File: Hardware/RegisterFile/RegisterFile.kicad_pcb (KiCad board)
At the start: 4 copper layers, 94 x 66 mm, 39 parts, among them J1 Conn_02x08_Odd_Even, J2 Conn_02x08_Odd_Even, J3 Conn_02x08_Odd_Even, J4 Conn_02x08_Odd_Even, U1 74LS138

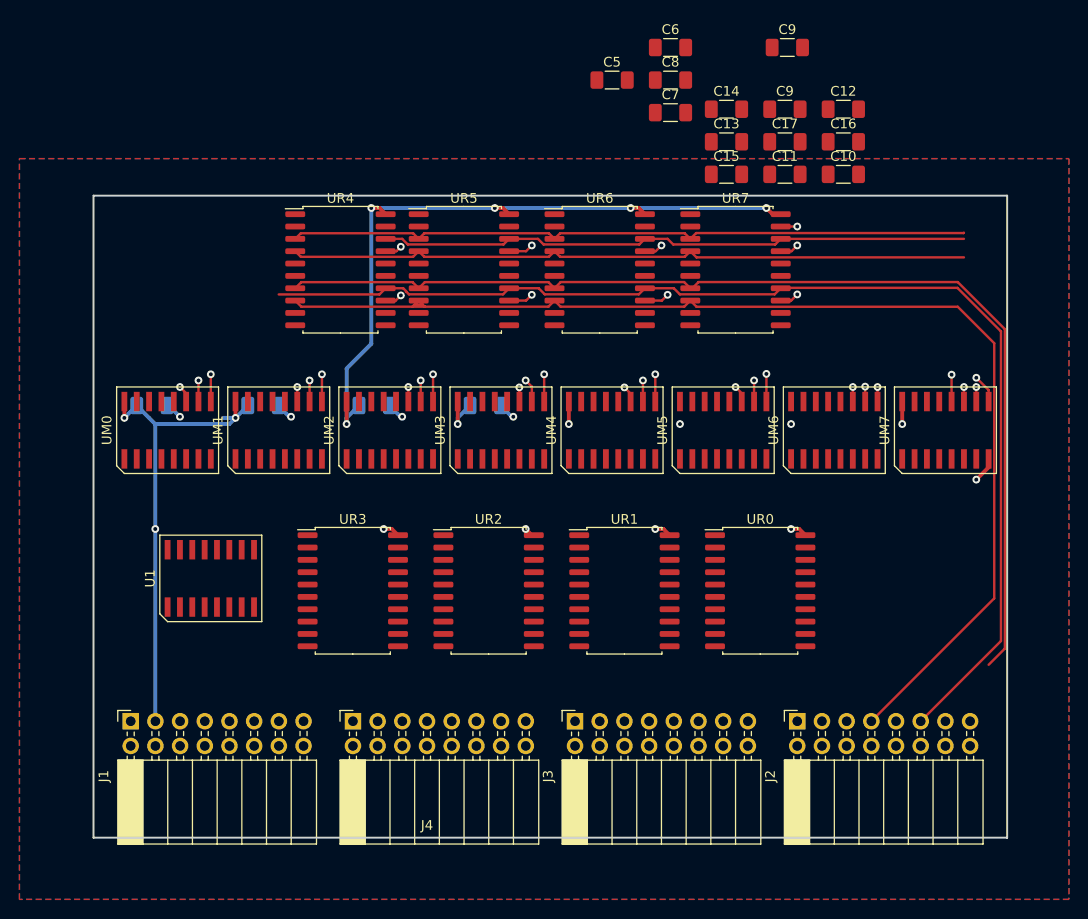
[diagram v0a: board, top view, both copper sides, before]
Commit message: RegisterFile Layout: Everything except the "spider" (routing the all 8 muxes each to all 8 registers might be non-trivial)
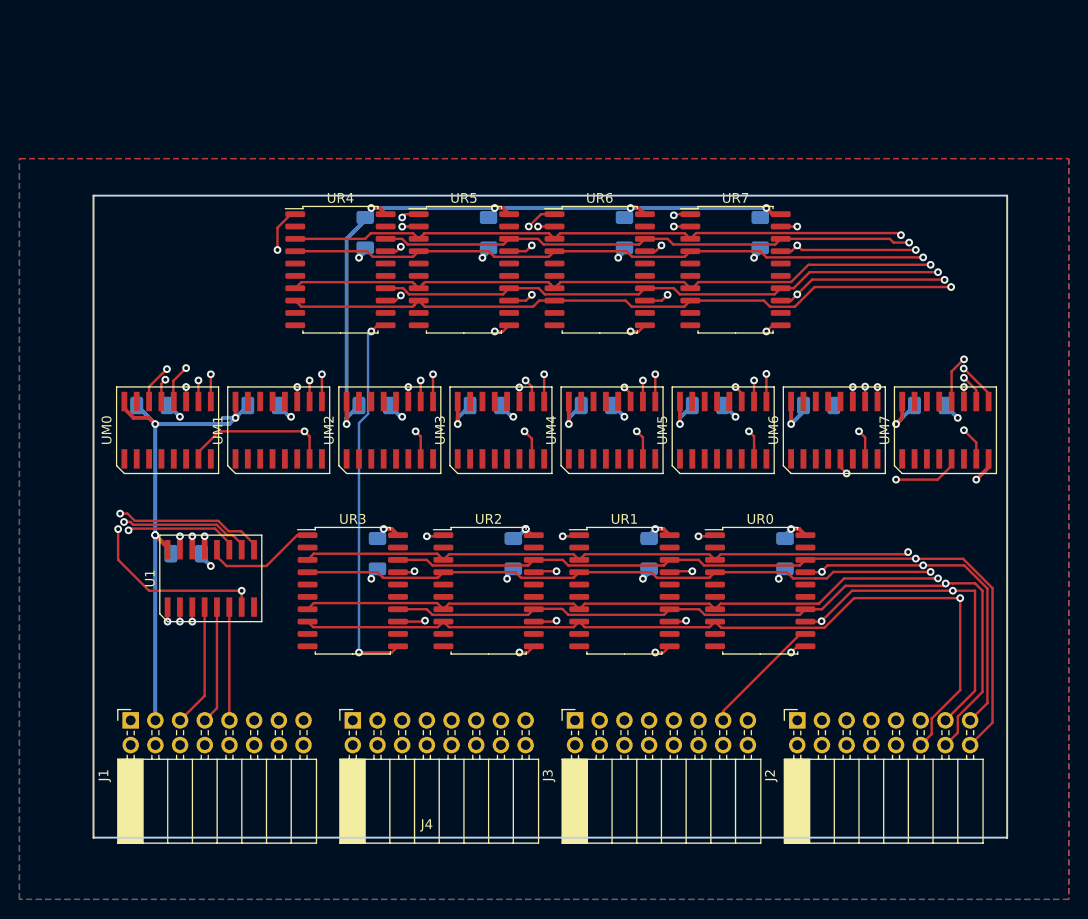
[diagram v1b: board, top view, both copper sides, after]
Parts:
- removed the C9 at (167.9, 52.1)
- removed the C9 at (167.6, 58.4)
- added C9: .1uF, Capacitor_SMD:C_1206_3216Metric_Pad1.33x1.80mm_HandSolder, B.Cu at (125.7, 104.1)
- C10, C11, C12, C13, C14, C15, C16, C17, C5, C6, C7, C8: moved to B.Cu
- moved C17 74.8 mm to (106.0, 104.1)
- moved C10 51.7 mm to (139.7, 104.1), turned to -90 degrees
- moved C12 46.1 mm to (167.6, 104.1), turned to -90 degrees
- moved C8 42.8 mm to (182.5, 88.9)
- moved C11 41.4 mm to (153.7, 104.1), turned to -90 degrees
- moved C13 38.3 mm to (124.5, 71.1), turned to -90 degrees
- moved C6 37.0 mm to (159.7, 88.9)
- moved C7 33.8 mm to (171.1, 88.9)
- moved C5 33.5 mm to (148.2, 88.9)
- moved C14 27.6 mm to (137.2, 71.1), turned to -90 degrees
- moved C16 12.7 mm to (165.1, 71.1), turned to -90 degrees
- moved C15 12.1 mm to (151.1, 71.1), turned to -90 degrees
- moved J4 0.09 mm to (123.2, 121.3)
- moved J1 0.09 mm to (100.3, 121.3)
- moved J2 0.09 mm to (168.9, 121.3)
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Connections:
- J2 pad 1: /DATAIN0 -> /DATAOUT0
- J2 pad 10: /DATAOUT4 -> /DATAIN1
- J2 pad 11: /DATAIN5 -> /DATAIN2
- J2 pad 12: /DATAOUT5 -> /DATAIN3
- J2 pad 13: /DATAIN6 -> /DATAIN4
- J2 pad 14: /DATAOUT6 -> /DATAIN5
- J2 pad 15: /DATAIN7 -> /DATAIN6
- J2 pad 16: /DATAOUT7 -> /DATAIN7
- J2 pad 2: /DATAOUT0 -> /DATAOUT1
- J2 pad 3: /DATAIN1 -> /DATAOUT2
- J2 pad 4: /DATAOUT1 -> /DATAOUT3
- J2 pad 5: /DATAIN2 -> /DATAOUT4
- J2 pad 6: /DATAOUT2 -> /DATAOUT5
- J2 pad 7: /DATAIN3 -> /DATAOUT6
- J2 pad 8: /DATAOUT3 -> /DATAOUT7
- J2 pad 9: /DATAIN4 -> /DATAIN0
- J3 pad 1: /REG0_0 -> /REG1_0
- J3 pad 10: /REG1_4 -> /REG0_1
- J3 pad 11: /REG0_5 -> /REG0_2
- J3 pad 12: /REG1_5 -> /REG0_3
- J3 pad 13: /REG0_6 -> /REG0_4
- J3 pad 14: /REG1_6 -> /REG0_5
- J3 pad 15: /REG0_7 -> /REG0_6
- J3 pad 16: /REG1_7 -> /REG0_7
- J3 pad 2: /REG1_0 -> /REG1_1
- J3 pad 3: /REG0_1 -> /REG1_2
- J3 pad 4: /REG1_1 -> /REG1_3
- J3 pad 5: /REG0_2 -> /REG1_4
- J3 pad 6: /REG1_2 -> /REG1_5
- J3 pad 7: /REG0_3 -> /REG1_6
- J3 pad 8: /REG1_3 -> /REG1_7
- J3 pad 9: /REG0_4 -> /REG0_0
- J4 pad 1: /REG2_0 -> /REG3_0
- J4 pad 10: /REG3_4 -> /REG2_1
- J4 pad 11: /REG2_5 -> /REG2_2
- J4 pad 12: /REG3_5 -> /REG2_3
- J4 pad 13: /REG2_6 -> /REG2_4
- J4 pad 14: /REG3_6 -> /REG2_5
- J4 pad 15: /REG2_7 -> /REG2_6
- J4 pad 16: /REG3_7 -> /REG2_7
- J4 pad 2: /REG3_0 -> /REG3_1
- J4 pad 3: /REG2_1 -> /REG3_2
- J4 pad 4: /REG3_1 -> /REG3_3
- J4 pad 5: /REG2_2 -> /REG3_4
- J4 pad 6: /REG3_2 -> /REG3_5
- J4 pad 7: /REG2_3 -> /REG3_6
- J4 pad 8: /REG3_3 -> /REG3_7
- J4 pad 9: /REG2_4 -> /REG2_0
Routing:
- net /CLK: track 0.00 -> 148.8 mm, vias 0 -> 8
- net /DATAIN1: track 70.5 -> 184.3 mm, vias 0 -> 2
- net /DATAIN6: track 66.2 -> 177.4 mm, vias 4 -> 10
- net /Regs/~{WRITESEL7}: track 0.00 -> 110.3 mm, vias 0 -> 3
- net /DATAIN7: track 60.9 -> 169.3 mm, vias 0 -> 2
- net /DATAIN0: track 70.5 -> 178.5 mm, vias 0 -> 2
- net /~{REN}: track 0.00 -> 102.3 mm, vias 0 -> 7
- net /Regs/~{WRITESEL6}: track 0.00 -> 81.8 mm, vias 0 -> 2
- net /DATAIN2: track 112.0 -> 183.6 mm, vias 0 -> 2
- net /DATAIN3: track 121.6 -> 189.6 mm, vias 0 -> 2
- net /Regs/~{WRITESEL5}: track 0.00 -> 64.8 mm, vias 0 -> 2
- net /DATAIN4: track 114.9 -> 179.2 mm, vias 4 -> 10
- net /REG7_0: track 0.00 -> 62.2 mm, vias 0 -> 2
- net /Regs/~{WRITESEL0}: track 0.00 -> 57.5 mm, vias 0 -> 2
- net /Regs/~{WRITESEL4}: track 0.00 -> 51.8 mm, vias 0 -> 2
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
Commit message: RegisterFile: The layout's all done!
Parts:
- added C18: .1uF, Capacitor_SMD:C_1206_3216Metric_Pad1.33x1.80mm_HandSolder, B.Cu at (101.6, 118.7)
- added C19: .1uF, Capacitor_SMD:C_1206_3216Metric_Pad1.33x1.80mm_HandSolder, B.Cu at (116.5, 118.7)
- J1, J2, J3, J4: footprint Connector_PinSocket_2.54mm:PinSocket_2x08_P2.54mm_Horizontal -> Connector_PinHeader_2.54mm:PinHeader_2x08_P2.54mm_Horizontal
- moved J2 17.8 mm to (186.7, 121.3), turned to -90 degrees
- moved J3 17.8 mm to (163.8, 121.3), turned to -90 degrees
- moved J4 17.8 mm to (141.0, 121.3), turned to -90 degrees
- moved J1 17.8 mm to (118.1, 121.3), turned to -90 degrees
- moved C12 6.35 mm to (174.0, 104.1)
- moved UR0 6.35 mm to (171.4, 108.0)
- moved C11 3.81 mm to (157.5, 104.1)
- moved UR1 3.81 mm to (154.9, 108.0)
- moved C10 1.27 mm to (141.0, 104.1)
- moved C9 1.27 mm to (124.5, 104.1)
- moved UR2 1.27 mm to (138.4, 108.0)
- moved UR3 1.27 mm to (121.9, 108.0)
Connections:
- J1 pad 10: /WRITEID1 -> /WRITEID0
- J1 pad 11: /CLK -> /~{WEN0}
- J1 pad 12: /WRITEID2 -> /READID2
- J1 pad 14: /~{REN} -> /READID1
- J1 pad 16: GND -> /READID0
- J1 pad 2: /READID0 -> GND
- J1 pad 4: /READID1 -> /~{REN}
- J1 pad 5: /~{WEN0} -> /CLK
- J1 pad 6: /READID2 -> /WRITEID2
- J1 pad 7: /~{WEN1} -> /WEN2
- J1 pad 8: /WRITEID0 -> /WRITEID1
- J1 pad 9: /WEN2 -> /~{WEN1}
- J2 pad 1: /DATAOUT0 -> /DATAIN6
- J2 pad 10: /DATAIN1 -> /DATAOUT7
- J2 pad 11: /DATAIN2 -> /DATAOUT4
- J2 pad 12: /DATAIN3 -> /DATAOUT5
- J2 pad 13: /DATAIN4 -> /DATAOUT2
- J2 pad 14: /DATAIN5 -> /DATAOUT3
- J2 pad 15: /DATAIN6 -> /DATAOUT0
- J2 pad 16: /DATAIN7 -> /DATAOUT1
- J2 pad 2: /DATAOUT1 -> /DATAIN7
- J2 pad 3: /DATAOUT2 -> /DATAIN4
- J2 pad 4: /DATAOUT3 -> /DATAIN5
- J2 pad 5: /DATAOUT4 -> /DATAIN2
- J2 pad 6: /DATAOUT5 -> /DATAIN3
- J2 pad 7: /DATAOUT6 -> /DATAIN0
- J2 pad 8: /DATAOUT7 -> /DATAIN1
- J2 pad 9: /DATAIN0 -> /DATAOUT6
- J3 pad 1: /REG1_0 -> /REG0_6
- J3 pad 10: /REG0_1 -> /REG1_7
- J3 pad 11: /REG0_2 -> /REG1_4
- J3 pad 12: /REG0_3 -> /REG1_5
- J3 pad 13: /REG0_4 -> /REG1_2
- J3 pad 14: /REG0_5 -> /REG1_3
- J3 pad 15: /REG0_6 -> /REG1_0
- J3 pad 16: /REG0_7 -> /REG1_1
- J3 pad 2: /REG1_1 -> /REG0_7
- J3 pad 3: /REG1_2 -> /REG0_4
- J3 pad 4: /REG1_3 -> /REG0_5
- J3 pad 5: /REG1_4 -> /REG0_2
- J3 pad 6: /REG1_5 -> /REG0_3
- J3 pad 7: /REG1_6 -> /REG0_0
- J3 pad 8: /REG1_7 -> /REG0_1
- J3 pad 9: /REG0_0 -> /REG1_6
- J4 pad 1: /REG3_0 -> /REG2_6
- J4 pad 10: /REG2_1 -> /REG3_7
- J4 pad 11: /REG2_2 -> /REG3_4
- J4 pad 12: /REG2_3 -> /REG3_5
- J4 pad 13: /REG2_4 -> /REG3_2
- J4 pad 14: /REG2_5 -> /REG3_3
- J4 pad 15: /REG2_6 -> /REG3_0
- J4 pad 16: /REG2_7 -> /REG3_1
- J4 pad 2: /REG3_1 -> /REG2_7
- J4 pad 3: /REG3_2 -> /REG2_4
- J4 pad 4: /REG3_3 -> /REG2_5
- J4 pad 5: /REG3_4 -> /REG2_2
- J4 pad 6: /REG3_5 -> /REG2_3
- J4 pad 7: /REG3_6 -> /REG2_0
- J4 pad 8: /REG3_7 -> /REG2_1
- J4 pad 9: /REG2_0 -> /REG3_6
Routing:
- net GND: track 27.0 -> 140.2 mm, vias 17 -> 36
- net /DATAOUT0: track 0.00 -> 106.5 mm, vias 0 -> 2
- net /DATAOUT1: track 0.00 -> 104.3 mm, vias 0 -> 1
- net /REG0_0: track 0.00 -> 88.8 mm, vias 0 -> 2
- net /DATAOUT2: track 0.00 -> 87.1 mm, vias 0 -> 1
- net /REG0_1: track 0.00 -> 83.6 mm, vias 0 -> 2
- net /REG3_7: track 0.00 -> 81.0 mm, vias 0 -> 3
- net /DATAOUT3: track 0.00 -> 79.6 mm, vias 0 -> 2
- net /REG4_7: track 0.00 -> 77.5 mm, vias 0 -> 2
- net /DATAOUT4: track 0.00 -> 76.8 mm, vias 0 -> 1
- net /REG1_0: track 0.00 -> 73.6 mm, vias 0 -> 2
- net /REG0_2: track 0.00 -> 70.2 mm, vias 0 -> 2
- net /REG3_6: track 0.00 -> 67.5 mm, vias 0 -> 3
- net /REG2_7: track 0.00 -> 64.5 mm, vias 0 -> 1
- net /REG1_1: track 0.00 -> 62.8 mm, vias 0 -> 2
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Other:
- board size 94 x 66 mm -> 94 x 60.3 mm
- board text added: "In"
- board text added: "Out"
- board text added: "Power,En,Sel,Clk"
- board text added: "Reg0"
- board text added: "Reg1"
- board text added: "Reg2"
- board text added: "Reg3"
- board text added: "Register File Made by Zane C datadeer.net/RRISC"
